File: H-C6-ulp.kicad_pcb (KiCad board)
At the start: 4 copper layers, 50.3 x 33 mm, 73 parts, among them J1 USB_C_Receptacle_USB2.0, J2 AFC24-S24FIC-00, J3 SM02B-SRSS-TB(LF)(SN), J4 SM04B-SRSS-TB_LF__SN_, Q1 Si1308, Q2 Si2301CDS, SW1 SW_Push_Dual, SW2 SW_Push_Dual, U1 ESP32-C6, U2 SGM6029CYG/TR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

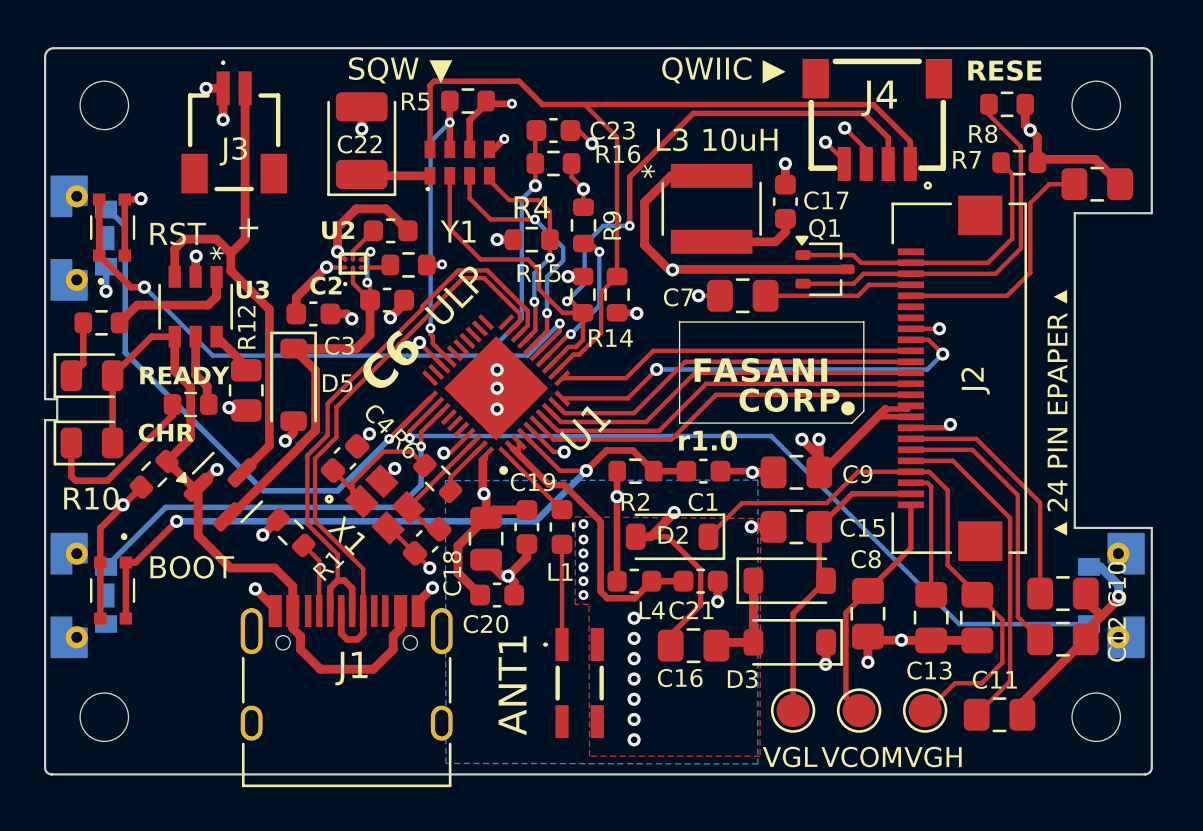
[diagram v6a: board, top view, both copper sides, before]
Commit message: Add pull-ups
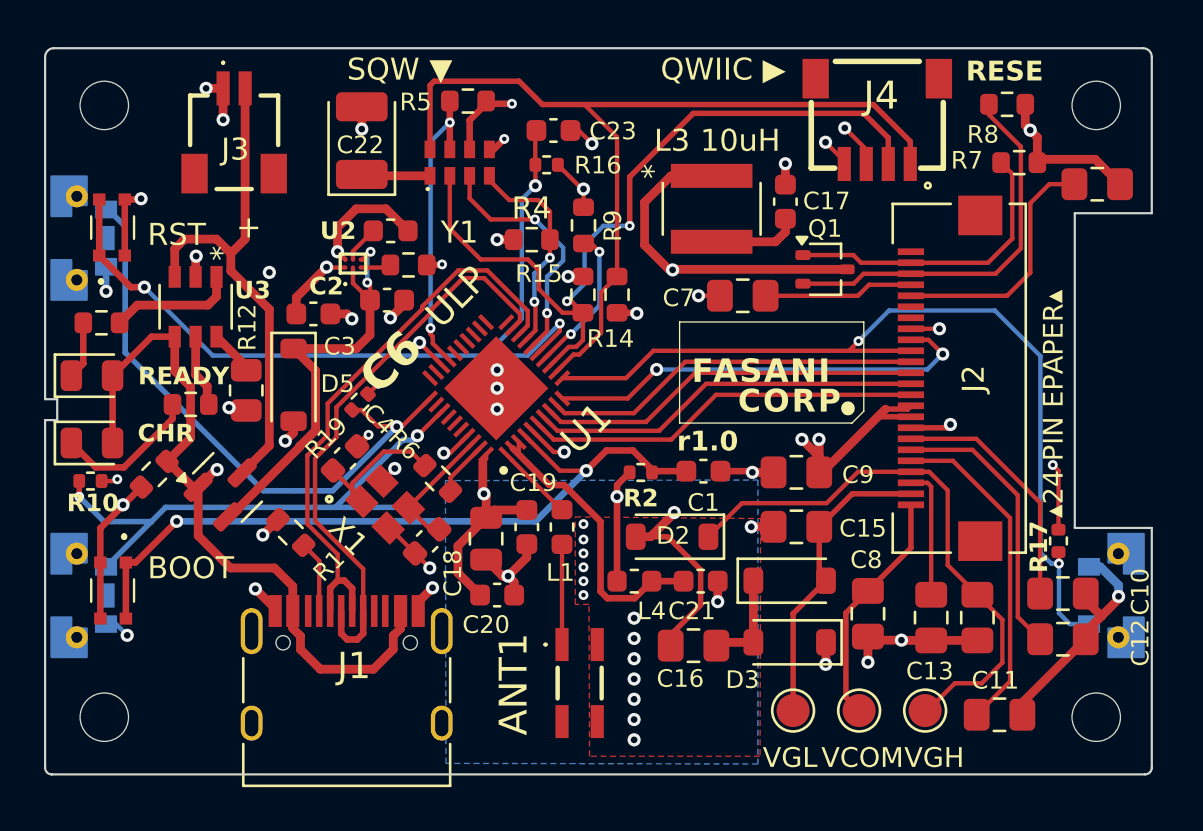
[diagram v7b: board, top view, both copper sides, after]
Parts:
- added R17: 10k, Resistor_SMD:R_0402_1005Metric, F.Cu at (164.3, 70.0)
- added R18: 10k, Resistor_SMD:R_0402_1005Metric, F.Cu at (120.3, 67.3)
- added R19: 10k, Resistor_SMD:R_0402_1005Metric, F.Cu at (132.5, 63.7)
- R16, R2: footprint Resistor_SMD:R_0603_1608Metric -> Resistor_SMD:R_0402_1005Metric
- moved R16 0.32 mm to (141.0, 52.9)
- moved R2 0.25 mm to (145.3, 66.9)
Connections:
- U1 pad 32: SW19 -> unconnected-(U1-GPIO19/SDIO_CLK/FSPICS3-Pad32)
- U5 pad 2: SW19 -> /EPD_RST
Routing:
- net SW19: track 36.5 -> 0.00 mm, vias 1 -> 0
- net /EPD_RST: track 16.4 -> 41.0 mm, vias 0 -> 2
- net VDD33: track 46.8 -> 67.3 mm, vias 15 -> 19
- net SW20: track 19.6 -> 25.6 mm, vias 1 -> 2
- net SW18: track 25.1 -> 27.4 mm
- net Net-(D6-K): track 7.93 -> 6.62 mm
- net GND: track 71.8 -> 72.9 mm, vias 49 -> 50
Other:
- board text added: "▴24 PIN EPAPER▴"
- board text removed: "▴ 24 PIN EPAPER ▴"

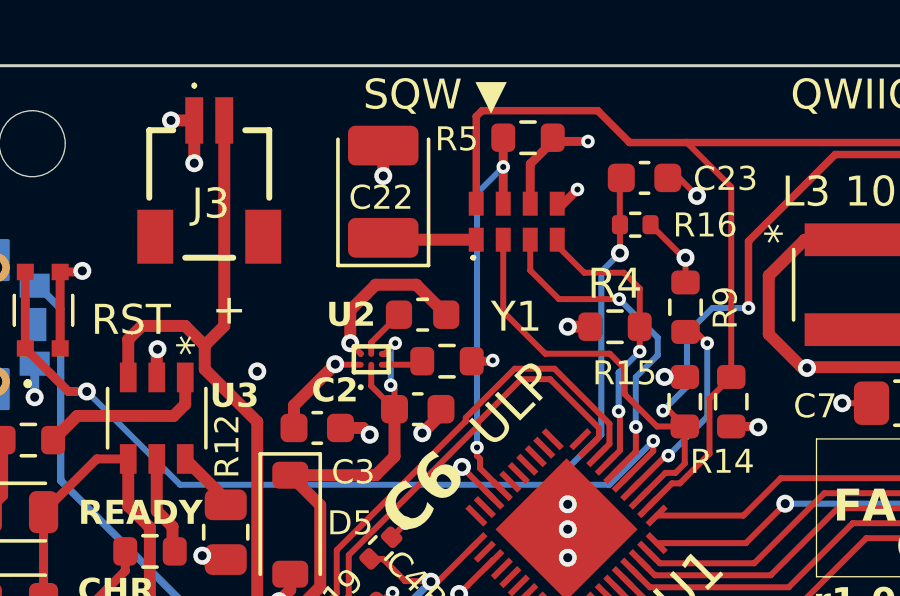
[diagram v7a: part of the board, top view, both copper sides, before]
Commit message: Update L2 with same inductor 470nH than XIAO C6
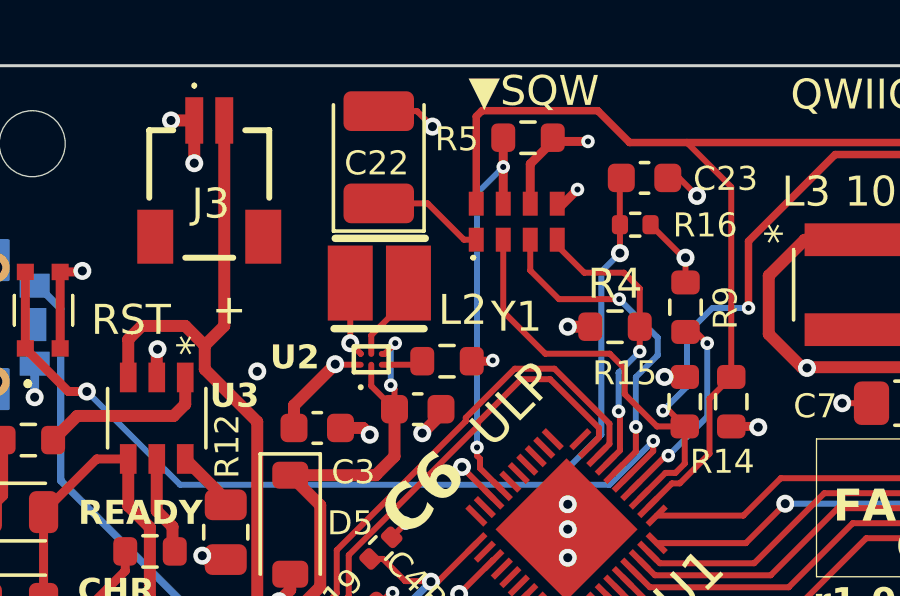
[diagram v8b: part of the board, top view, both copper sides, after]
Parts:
- L2: footprint Inductor_SMD:L_0603_1608Metric -> footprints:IND-SMD_L2.5-W2.0_SPH252012
- moved L2 1.79 mm to (132.5, 54.8), turned to 180 degrees
- moved C22 1.16 mm to (132.4, 50.7)
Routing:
- net VDD33: track 67.3 -> 64.3 mm
- net Net-(U2-SW): track 1.69 -> 2.88 mm
- net GND: track 72.9 -> 73.9 mm
- net VDD_RTC: track 3.13 -> 3.75 mm
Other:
- board text added: "▼SQW"
- board text removed: "SQW ▼"
